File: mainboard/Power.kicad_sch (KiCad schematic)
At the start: 32 parts, among them IC801 TPS62823DLC, IC802 LP5907MFX-2.8, IC803 LP5907MFX-1.5, IC804 LP5907MFX-3.0, IC805 LP5907MFX-2.8, IC806 LP5907MFX-1.2

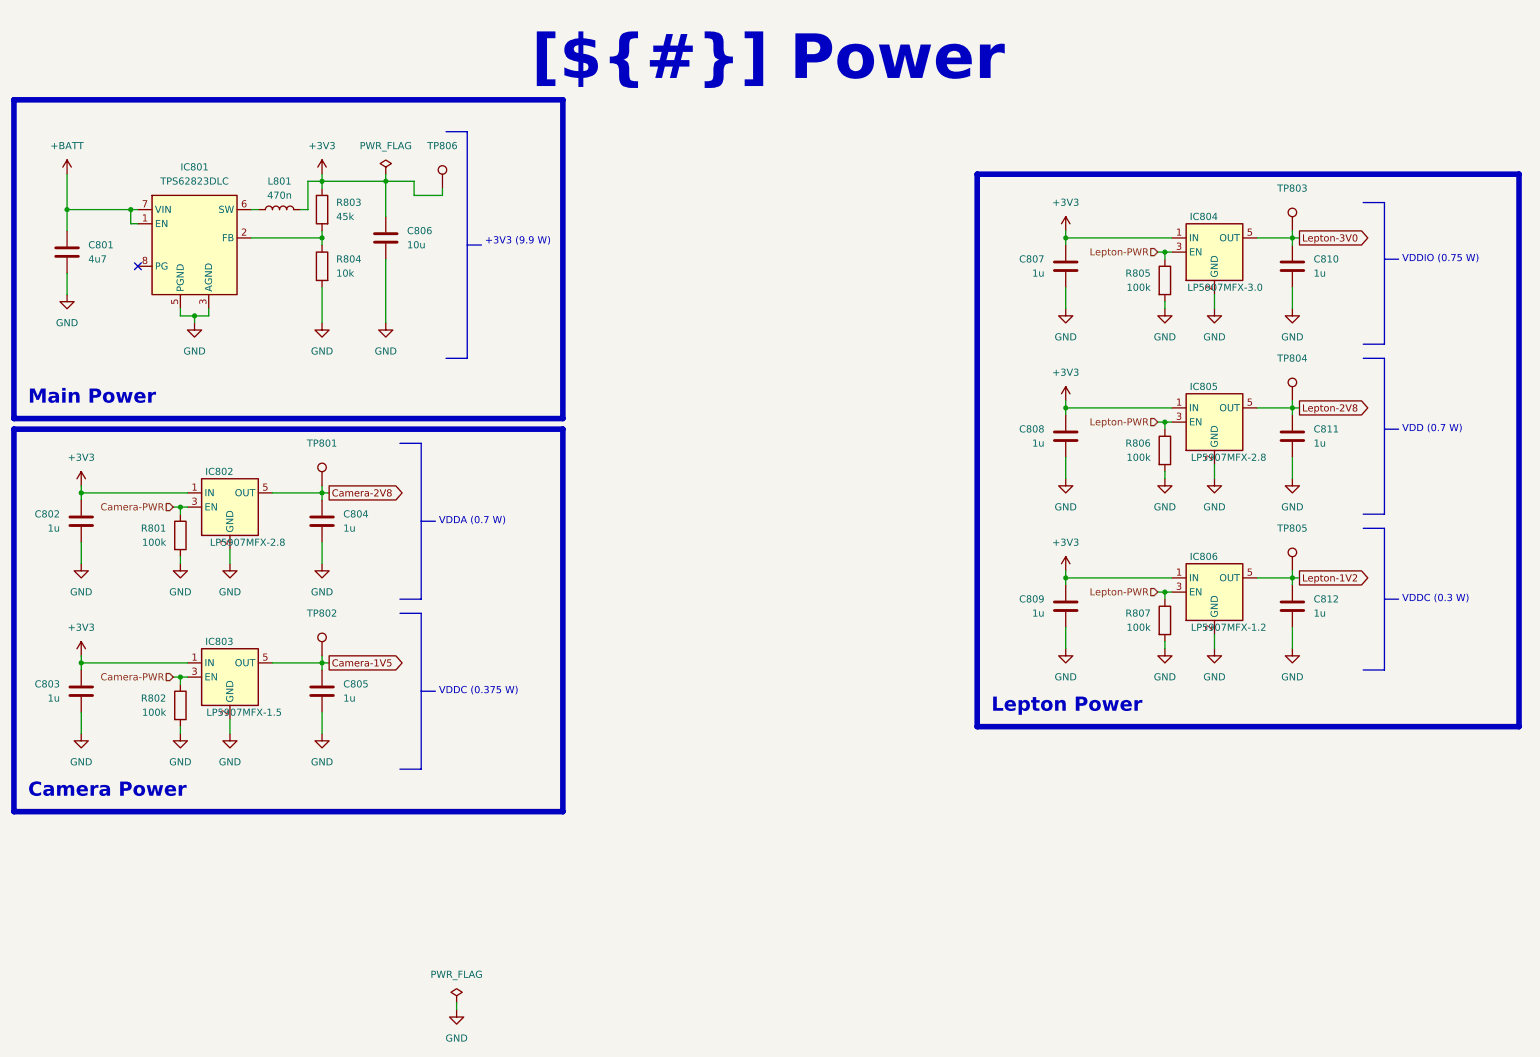
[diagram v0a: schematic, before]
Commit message: Replace temperature sensor and optimize the position, replace LiPo battery with a flat one
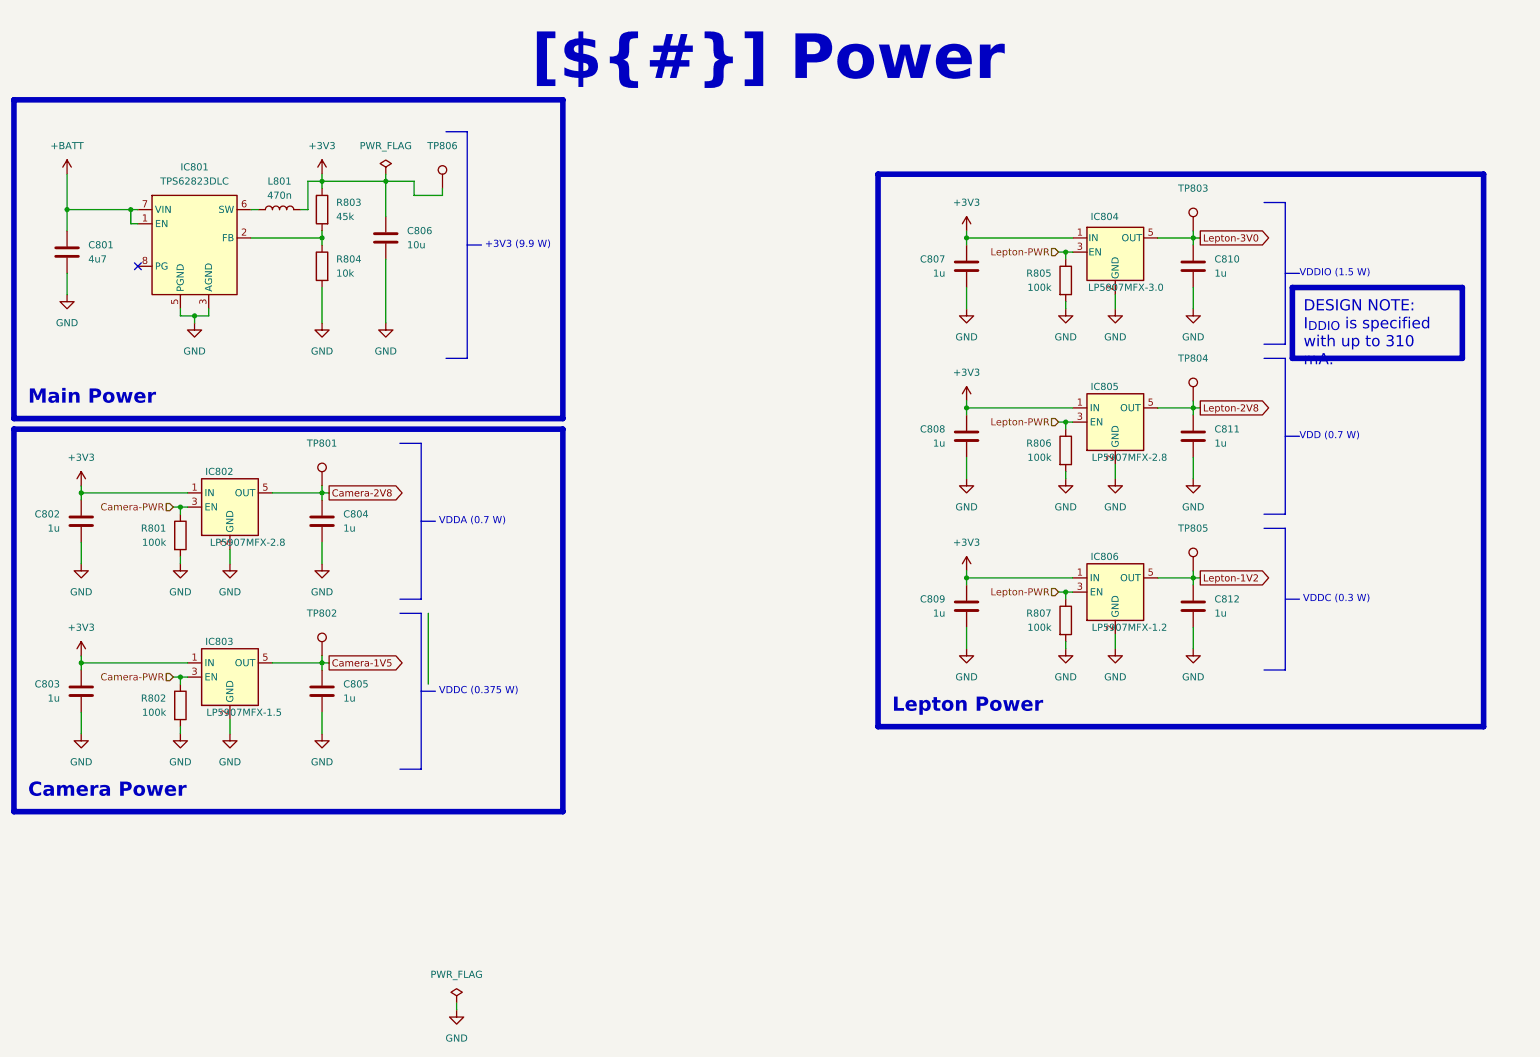
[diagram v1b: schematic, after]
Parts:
- IC804: symbol Regulator_Linear:LP5907MFX-3.0 -> Regulator_Linear:TLV75530PDBV; manf# LP5907MFX-3.0 -> TLV75530PDBVR; mouser# 595-LP5907MFX-3.0 -> 595-TLV75530PDBVR
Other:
- note added: "VDDIO (1.5 W)"
- note removed: "VDDIO (0.75 W)"
- moved on the sheet: C807, C808, C809, C810, C811, C812, IC804, IC805, IC806, R805, R806, R807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

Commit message: Layout complete
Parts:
- added R808: 100k, Resistor_SMD:R_0603_1608Metric, symbol Device:R
- added SW701: On / Off, Button_Switch_THT:SW_Slide_SPDT_Angled_CK_OS102011MA1Q, symbol Switch:SW_SPDT
- renumbered TP806 to TP803, TP803 to TP804, TP804 to TP805, TP805 to TP806
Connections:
- net +BATT: now also SW701.3 (C); no longer IC801.1 (EN)
- net GND: now also R808.2
- new net: IC801.1 (EN), SW701.2 (B)
- new net: R808.1, SW701.1 (A)
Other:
- moved on the sheet: C801, C802, C803, C804, C805, C806, IC801, IC802, IC803, L801, R801, R802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

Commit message: Release 1.0.0
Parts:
- TP801, TP802, TP803, TP804, TP805, TP806: footprint TestPoint:TestPoint_Pad_1.0x1.0mm -> Testpoints_Kampi:TestPoint_Pad_1.0x1.0mm
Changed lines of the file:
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@@
 			)
 		)
-		(property "Footprint" "TestPoint:TestPoint_Pad_1.0x1.0mm"
+		(property "Footprint" "Testpoints_Kampi:TestPoint_Pad_1.0x1.0mm"
 			(at 111.76 113.03 0)
 			(effects
@@
 			)
 		)
-		(property "Footprint" "TestPoint:TestPoint_Pad_1.0x1.0mm"
+		(property "Footprint" "Testpoints_Kampi:TestPoint_Pad_1.0x1.0mm"
 			(at 229.87 81.28 0)
 			(effects
@@
 			)
 		)
-		(property "Footprint" "TestPoint:TestPoint_Pad_1.0x1.0mm"
+		(property "Footprint" "Testpoints_Kampi:TestPoint_Pad_1.0x1.0mm"
 			(at 73.66 34.29 0)
 			(effects
@@
 			)
 		)
-		(property "Footprint" "TestPoint:TestPoint_Pad_1.0x1.0mm"
+		(property "Footprint" "Testpoints_Kampi:TestPoint_Pad_1.0x1.0mm"
 			(at 229.87 111.76 0)
 			(effects
@@
 			)
 		)
-		(property "Footprint" "TestPoint:TestPoint_Pad_1.0x1.0mm"
+		(property "Footprint" "Testpoints_Kampi:TestPoint_Pad_1.0x1.0mm"
 			(at 229.87 50.8 0)
 			(effects
@@
 			)
 		)
-		(property "Footprint" "TestPoint:TestPoint_Pad_1.0x1.0mm"
+		(property "Footprint" "Testpoints_Kampi:TestPoint_Pad_1.0x1.0mm"
 			(at 73.66 67.31 0)
 			(effects

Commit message: Task: Issue #7
- Increase the width of the cutout for the temperature sensor
- Add missing component informations
- Fix wrong component informations

Closes: #7

Signed-off-by: Daniel Kampert <DanielKampert@kampis-elektroecke.de>
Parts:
- R804: manf Bourns -> YAGEO; manf# CR0603-JW-103ELF -> RC0603FR-073K3L; mouser# 652-CR0603-JW-103ELF -> 603-RC0603FR-073K3L
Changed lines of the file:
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@@
 			)
 		)
-		(property "manf" "Bourns"
+		(property "manf" "YAGEO"
 			(at 85.09 127 0)
 			(effects
@@
 			)
 		)
-		(property "manf#" "CR0603-JW-103ELF"
+		(property "manf#" "RC0603FR-073K3L"
 			(at 85.09 127 0)
 			(effects
@@
 			)
 		)
-		(property "mouser#" "652-CR0603-JW-103ELF"
+		(property "mouser#" "603-RC0603FR-073K3L"
 			(at 85.09 127 0)
 			(effects

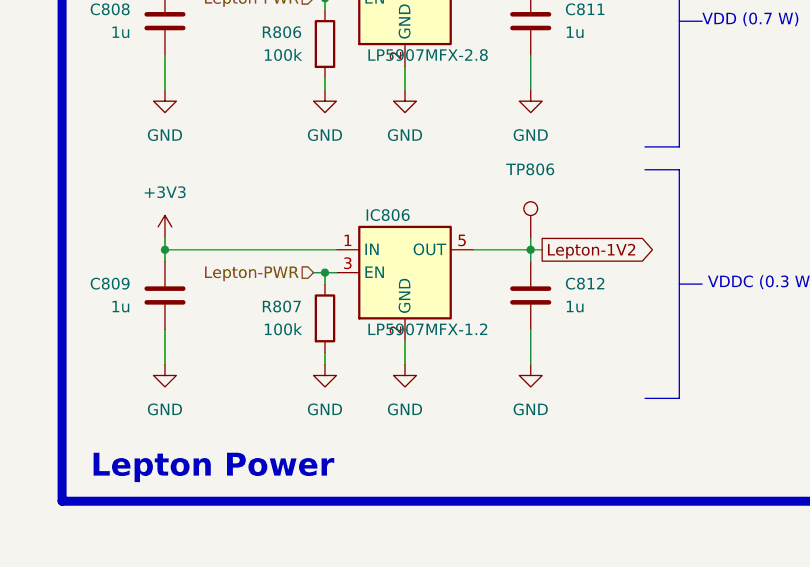
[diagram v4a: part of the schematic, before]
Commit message: Add feedback from PCBWay
Signed-off-by: Daniel Kampert <DanielKampert@kampis-elektroecke.de>
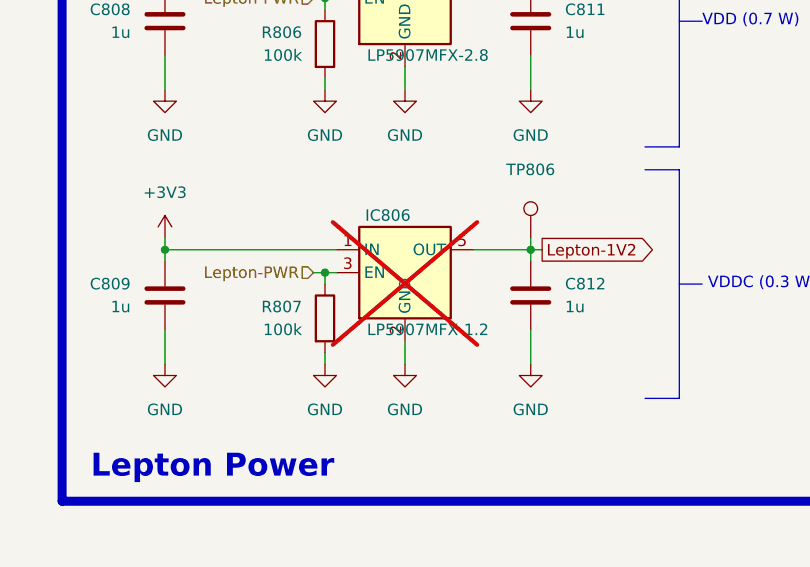
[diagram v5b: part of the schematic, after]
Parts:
- IC803: manf# LP5907MFX1.5NOPB -> LP5907MFX-1.5/NOPB; mouser# 595-LP5907MFX1.5NOPB -> 595-LP5907MFX-1.5/NOPB
- IC806: now not fitted
- SW701: manf# OS102011MA1Q -> OS102011MA1QN1; mouser# 611-OS102011MA1Q -> 611-OS102011MA1QN1
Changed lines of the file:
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@@
 			)
 		)
-		(property "manf#" " LP5907MFX1.5NOPB"
+		(property "manf#" "LP5907MFX-1.5/NOPB"
 			(at 52.07 71.12 0)
 			(effects
@@
 			)
 		)
-		(property "mouser#" " 595-LP5907MFX1.5NOPB"
+		(property "mouser#" "595-LP5907MFX-1.5/NOPB"
 			(at 52.07 71.12 0)
 			(effects
@@
 		(in_bom yes)
 		(on_board yes)
-		(dnp no)
+		(dnp yes)
 		(property "Reference" "IC806"
 			(at 208.915 109.22 0)
@@
 			)
 		)
-		(property "manf#" "OS102011MA1Q"
+		(property "manf#" "OS102011MA1QN1"
 			(at 39.37 128.27 0)
 			(effects
@@
 			)
 		)
-		(property "mouser#" "611-OS102011MA1Q"
+		(property "mouser#" "611-OS102011MA1QN1"
 			(at 39.37 128.27 0)
 			(effects

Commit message: Bug: Fixing several component issues
Closes: #17
Closes: #16
Closes: #15
Closes: #14
Closes: #13
Closes: #12

Signed-off-by: Daniel Kampert <danielkampert@kampis-elektroecke.de>
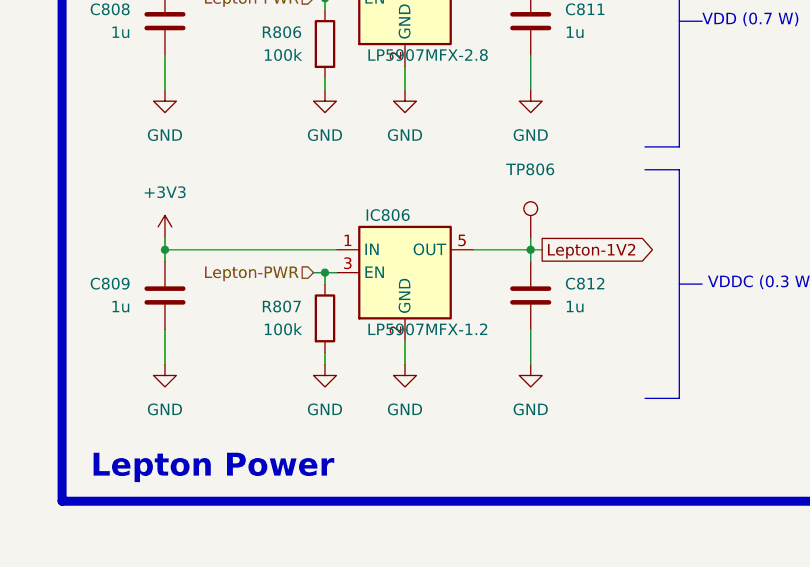
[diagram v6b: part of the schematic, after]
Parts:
- IC801: manf# TPS62823DLCT -> TPS62823DLCR; mouser# 595-TPS62823DLCT -> 595-TPS62823DLCR
- IC804: manf# TLV75530PDBVR -> LP5907MFX-3.0/NOPB; mouser# 595-TLV75530PDBVR -> 595-LP5907MFX-3.0NPB
- IC806: now fitted
- L801: manf# DFE201610E - R47M -> DFE201610E-R47M=P2; mouser# 81-DFE201610E - R47M -> 81-DFE201610E-R47MP2
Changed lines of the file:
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@@
 			)
 		)
-		(property "manf#" "TPS62823DLCT"
+		(property "manf#" "TPS62823DLCR"
 			(at 62.23 124.46 0)
 			(effects
@@
 			)
 		)
-		(property "mouser#" "595-TPS62823DLCT"
+		(property "mouser#" "595-TPS62823DLCR"
 			(at 62.23 124.46 0)
 			(effects
@@
 			)
 		)
-		(property "manf#" "TLV75530PDBVR"
+		(property "manf#" "LP5907MFX-3.0/NOPB"
 			(at 210.82 54.61 0)
 			(effects
@@
 			)
 		)
-		(property "mouser#" "595-TLV75530PDBVR"
+		(property "mouser#" "595-LP5907MFX-3.0NPB"
 			(at 210.82 54.61 0)
 			(effects
@@
 			)
 		)
-		(property "manf#" "DFE201610E - R47M"
+		(property "manf#" "DFE201610E-R47M=P2"
 			(at 77.47 116.84 0)
 			(effects
@@
 			)
 		)
-		(property "mouser#" "81-DFE201610E - R47M"
+		(property "mouser#" "81-DFE201610E-R47MP2"
 			(at 77.47 116.84 0)
 			(effects
@@
 		(in_bom yes)
 		(on_board yes)
-		(dnp yes)
+		(dnp no)
 		(property "Reference" "IC806"
 			(at 208.915 109.22 0)

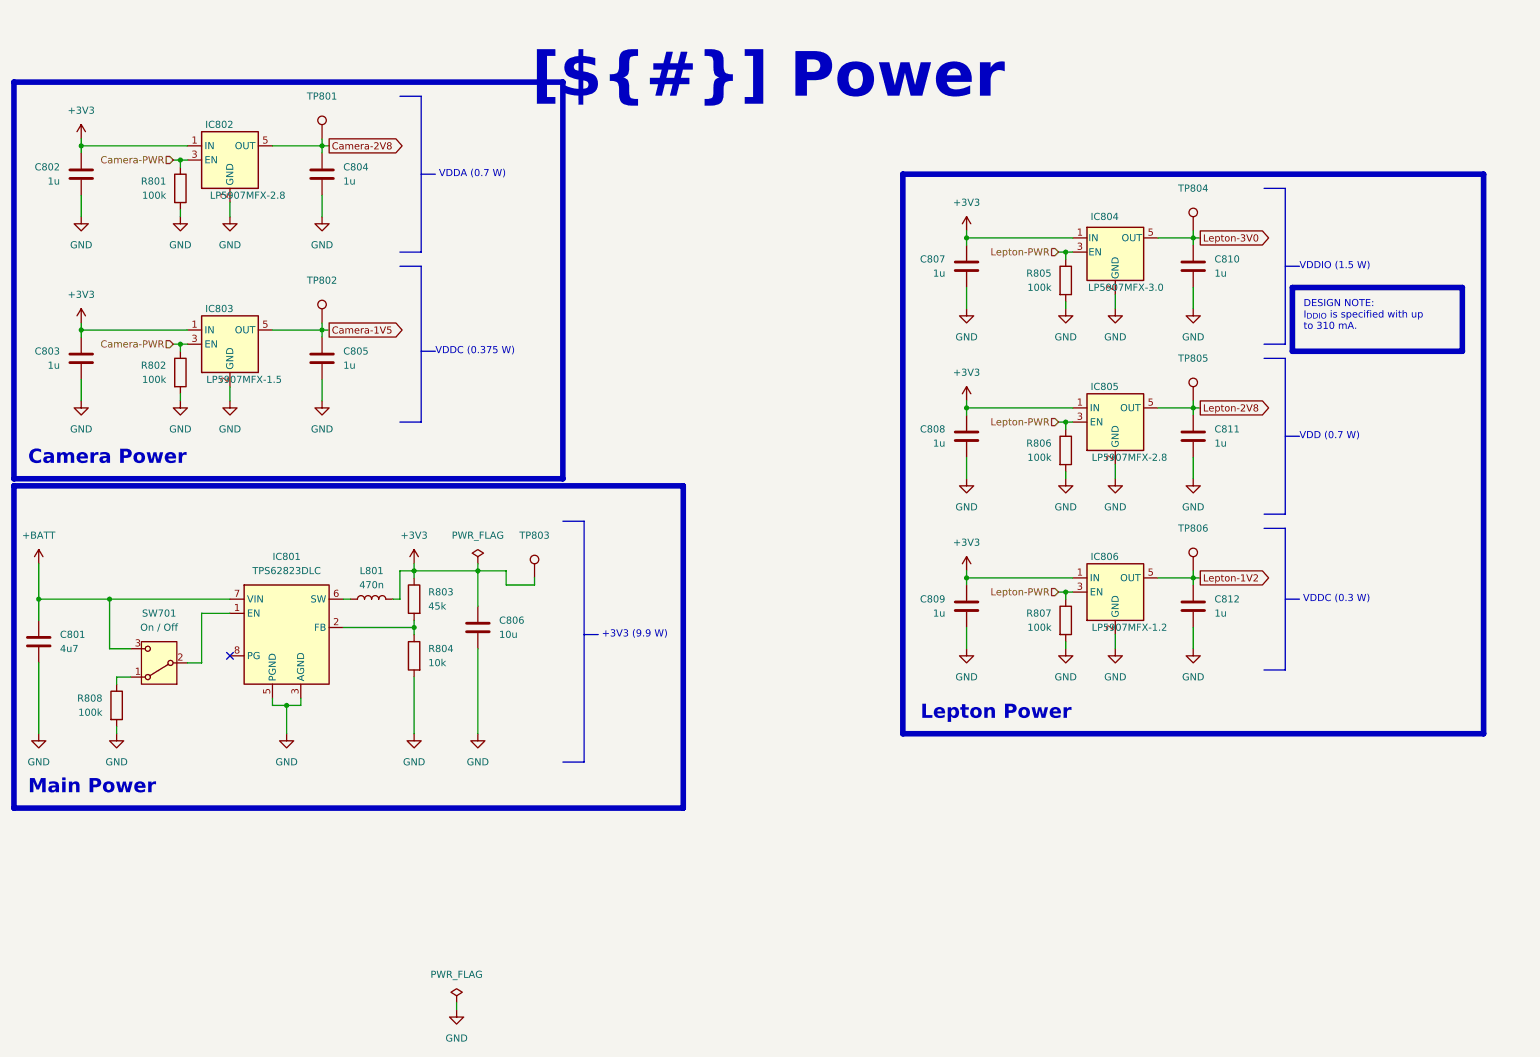
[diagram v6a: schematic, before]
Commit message: Add VL53L1X ToF sensor
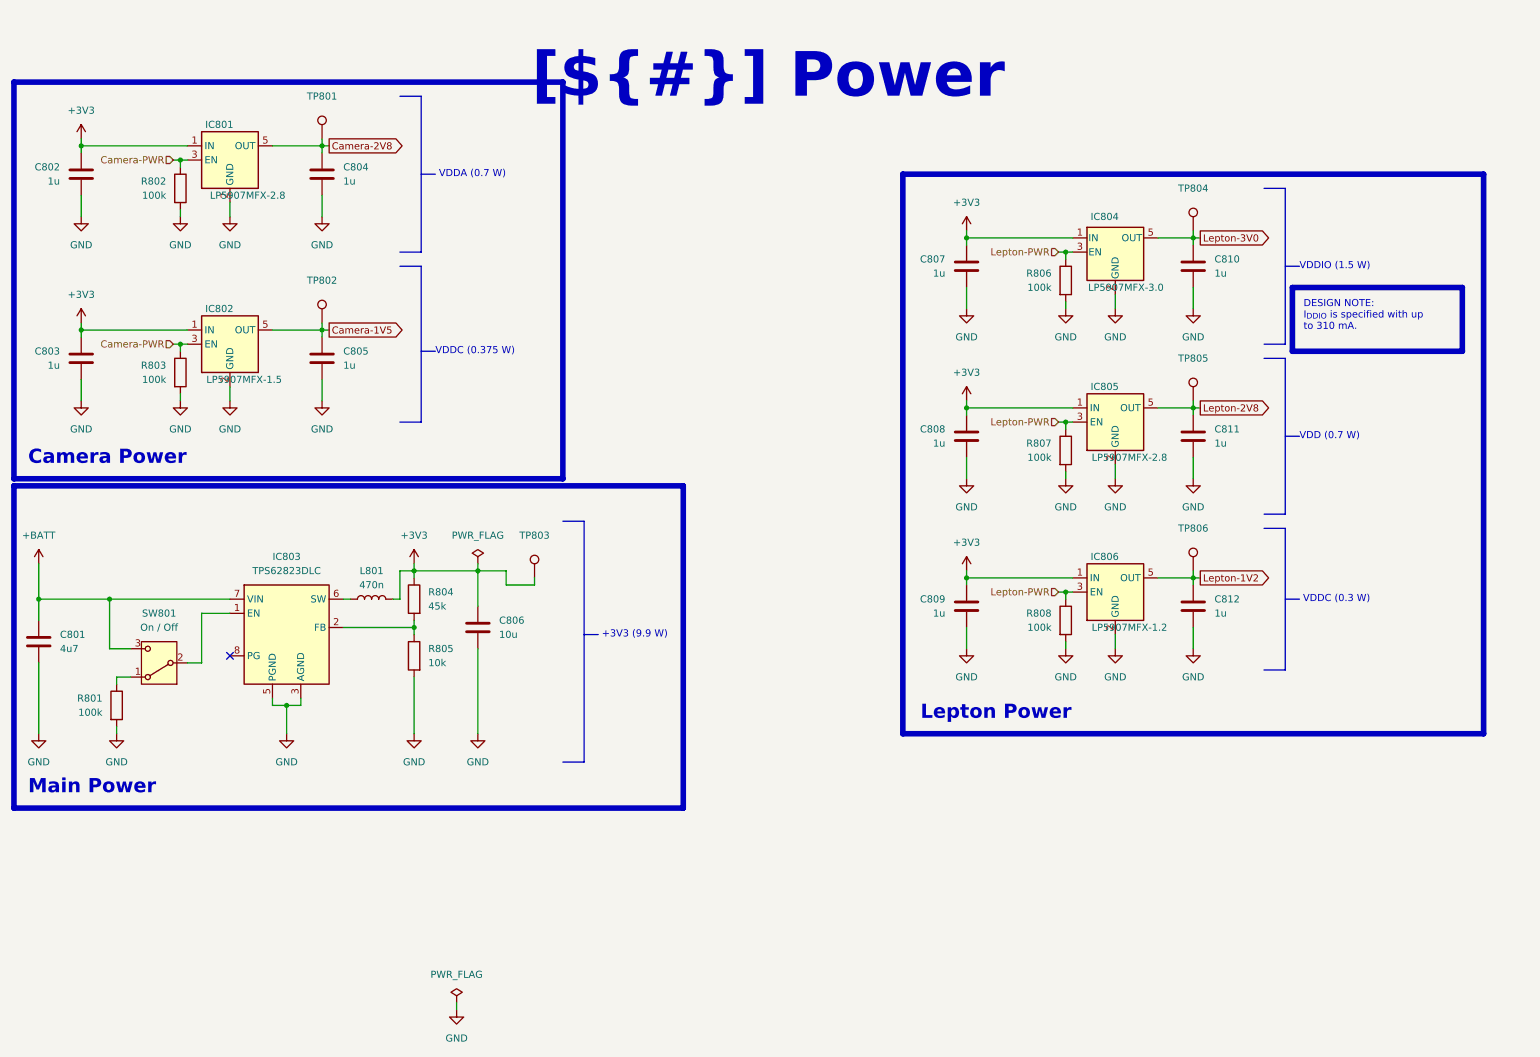
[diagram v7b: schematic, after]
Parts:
- renumbered IC802 to IC801, IC803 to IC802, IC801 to IC803, R808 to R801, R801 to R802, R802 to R803, R803 to R804, R804 to R805, R805 to R806, R806 to R807, R807 to R808, SW701 to SW801
